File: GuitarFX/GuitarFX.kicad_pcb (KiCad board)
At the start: 4 copper layers, 70 x 85 mm, 125 parts, among them IC401 PCM3060PWR, J202 Screw_Terminal_01x02, J301 USB_C_Receptacle_USB2.0, J302 Conn_ARM_SWD_TagConnect_TC2030, J303 Screw_Terminal_01x06, J401 Screw_Terminal_01x02, J402 Screw_Terminal_01x02, SW301 SW_SPDT, U201 NCP718xSN500, U202 NCP1117-3.3_SOT223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

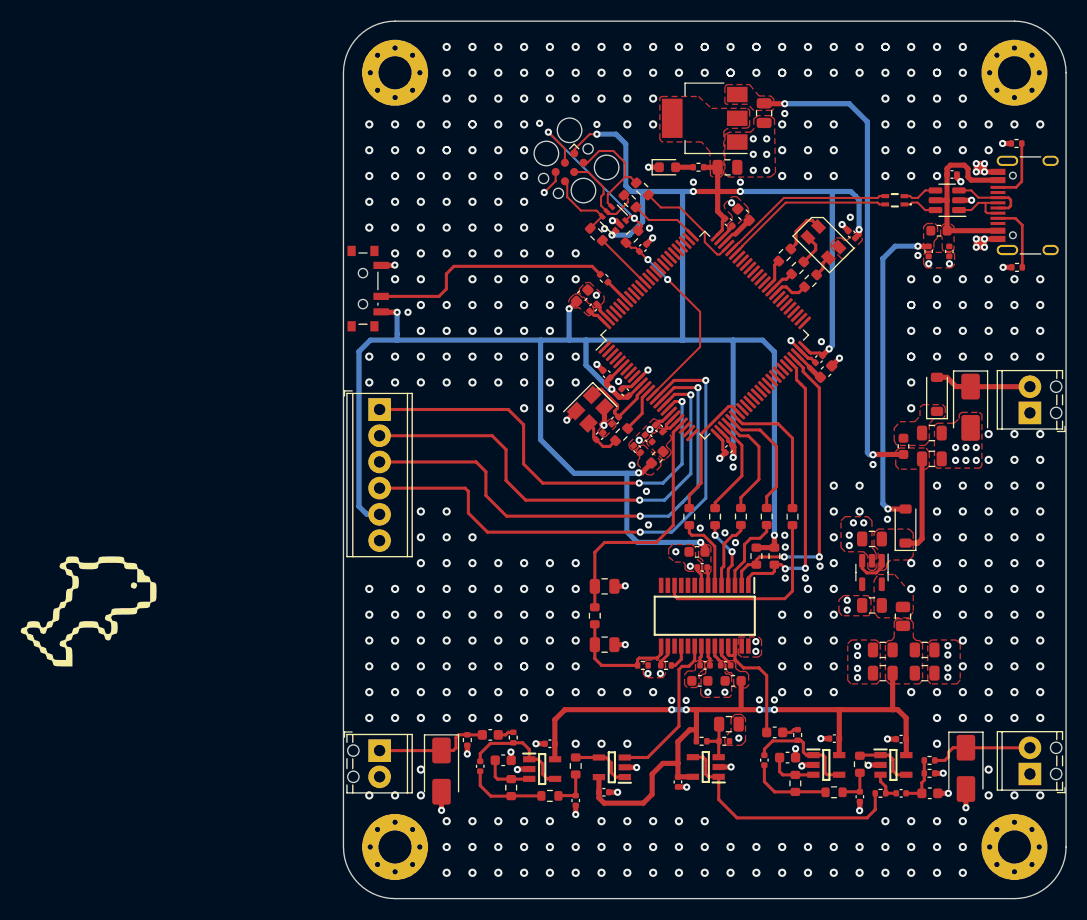
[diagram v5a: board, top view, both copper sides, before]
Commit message: Added silkscreen and tidied up component positioning
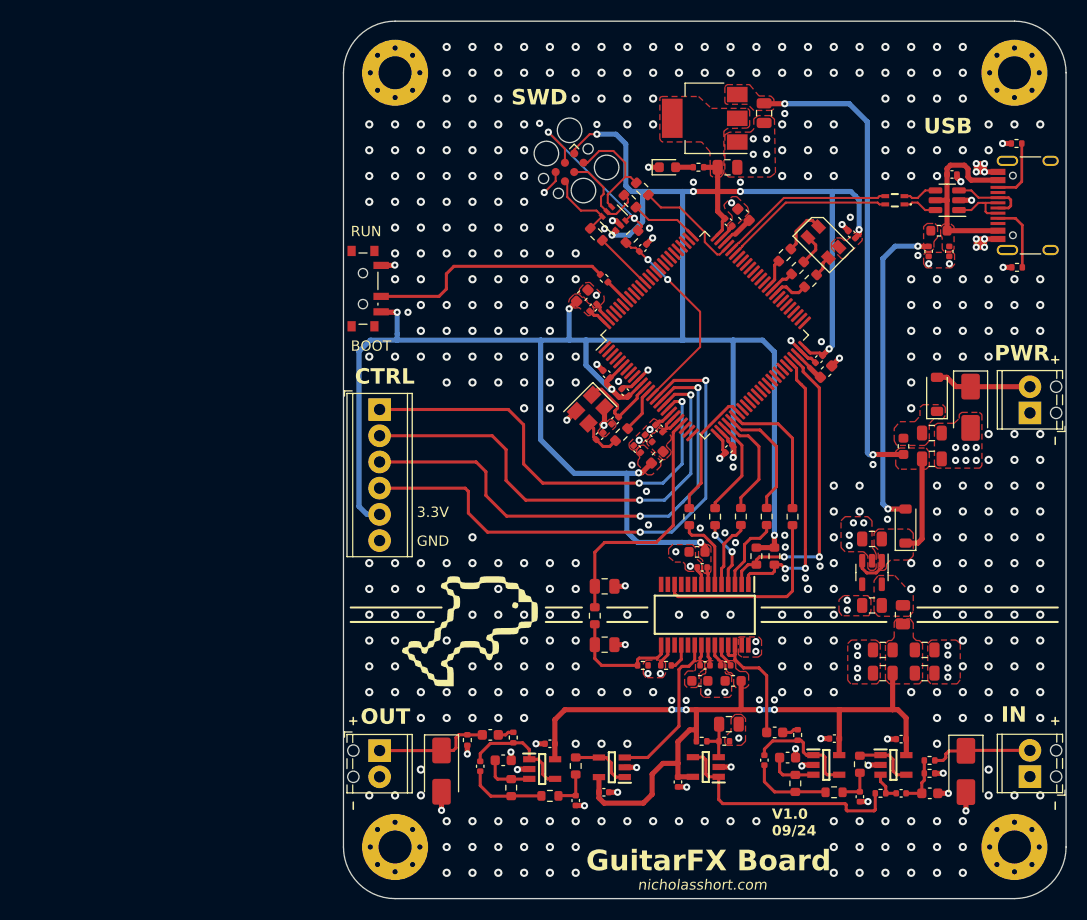
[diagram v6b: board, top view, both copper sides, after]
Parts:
- moved G*** 37.0 mm to (121.9, 120.4)
- moved D401 0.30 mm to (170.3, 131.2)
- moved J401 0.25 mm to (176.5, 131.7)
- moved R201 0.16 mm to (164.2, 116.0)
- moved IC401 0.10 mm to (145.0, 116.0)
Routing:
- net GND: track 75.0 -> 74.9 mm, vias 533 -> 486
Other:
- board text added: "3.3V"
- board text added: "BOOT"
- board text added: "CTRL"
- board text added: "GND"
- board text added: "GuitarFX Board"
- board text added: "IN"
- board text added: "OUT"
- board text added: "PWR"
- board text added: "RUN"
- board text added: "SWD"
- board text added: "USB"
- board text added: "V1.0 09/24"
- board text added: "nicholasshort.com"
